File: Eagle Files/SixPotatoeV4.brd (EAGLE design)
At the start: 120 x 60 mm, 27 parts, among them J3 IMU, J4 ON/OFF, J5 GND, J6 3.3v

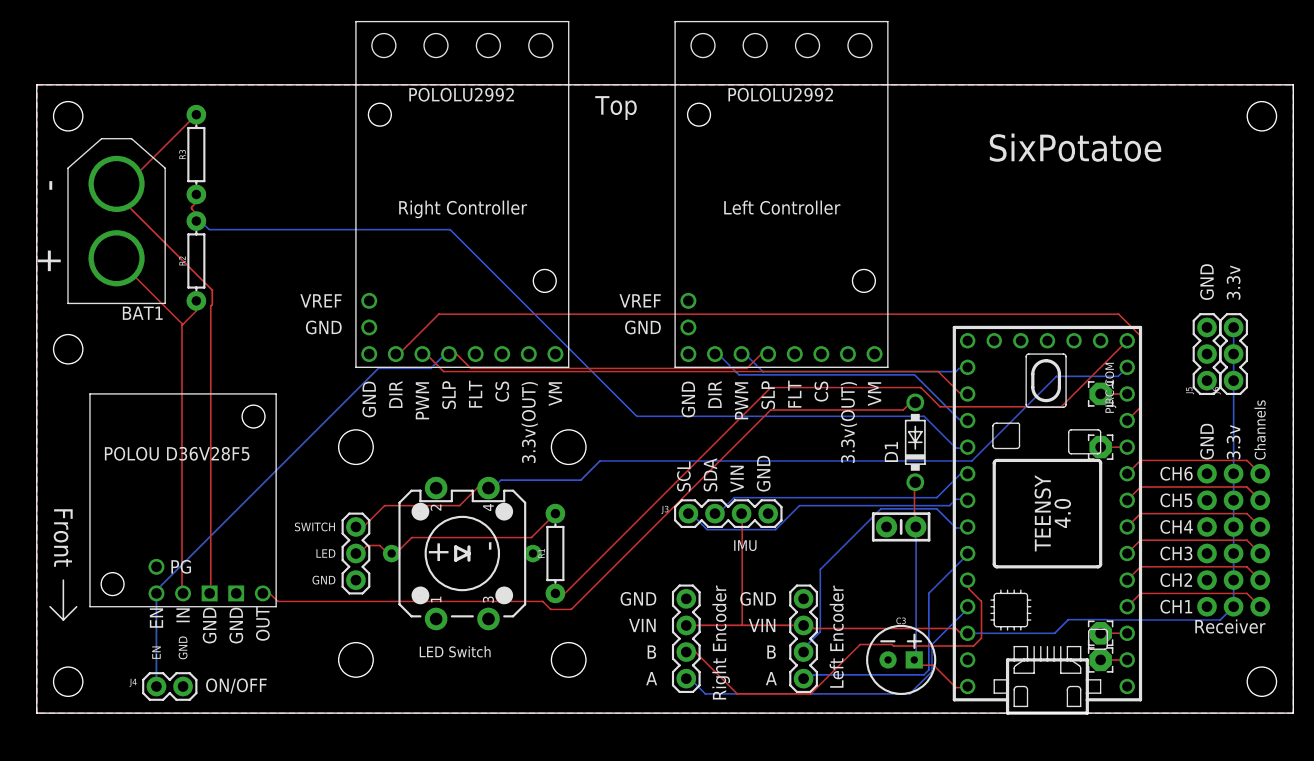
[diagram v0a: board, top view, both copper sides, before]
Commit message: Video completed
Also, excess code removed, first routes checked out.
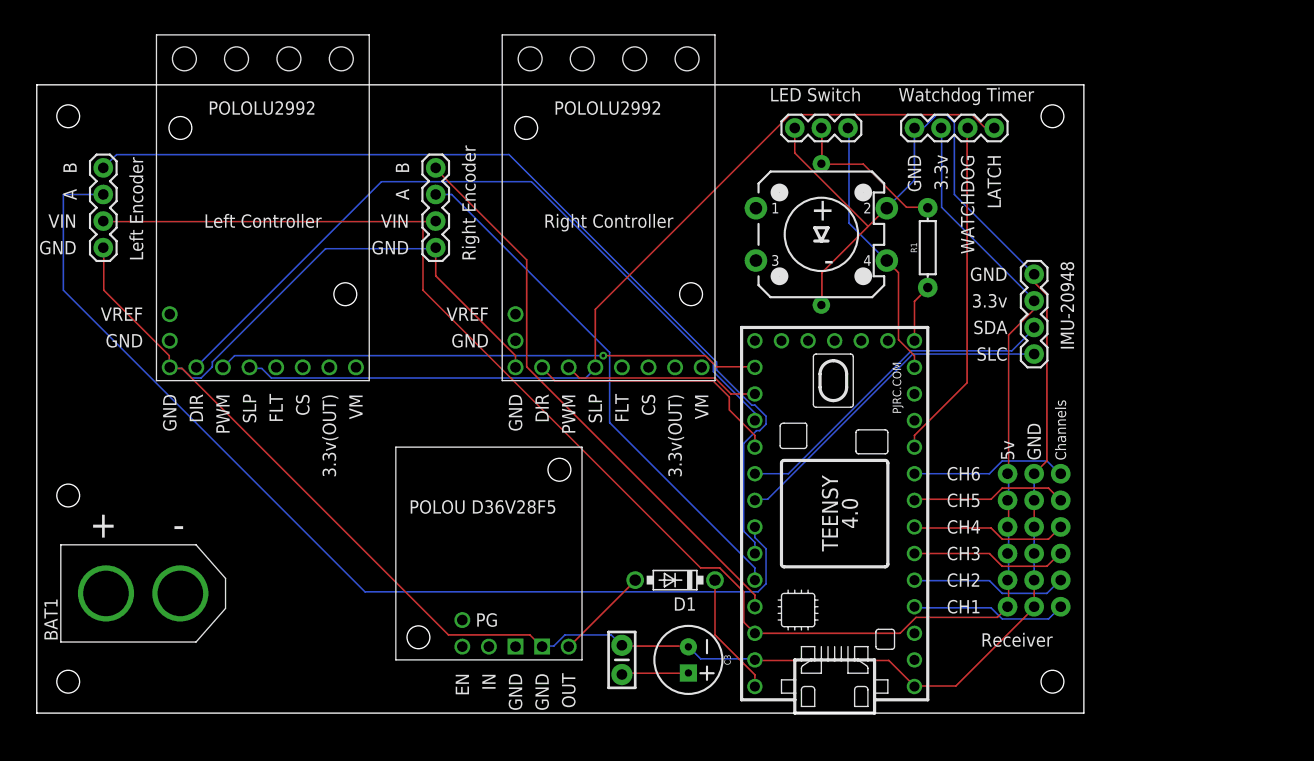
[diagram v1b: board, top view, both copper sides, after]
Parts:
- removed 0, 1, 10, 8: (no value), wirepad:2,15/1,0
- removed J4: ON/OFF, SparkFun-Connectors:1X02
- removed J5: GND, SparkFun-Connectors:1X03
- removed J6: 3.3v, SparkFun-Connectors:1X03
- removed R2, R3: 15k, SparkFun-Resistors:AXIAL-0.3
- removed U$5: SEN15335_NO_PTH, TimEagleLibrary:SEN15335_NO_PTH
- added J7: (no value), SparkFun-Connectors:1X04
- J3: value IMU -> (none)
- moved J2 74.8 mm to (6.35, 44.5), turned to 90 degrees
- moved J19 60.5 mm to (77.5, 55.9), turned to 180 degrees
- moved U$2 49.5 mm to (31.8, 64.8)
- moved R1 46.0 mm to (85.1, 44.5)
- moved S2 45.9 mm to (74.9, 45.7), turned to 0 degrees
- moved J1 41.2 mm to (38.1, 44.5), turned to 90 degrees
- moved J3 40.2 mm to (95.2, 41.9), turned to 270 degrees
- moved BAT1 35.7 mm to (10.2, 11.4), turned to 180 degrees
- moved U$4 29.6 mm to (43.2, 14.0)
- moved C2 29.5 mm to (55.9, 5.08), turned to 270 degrees
- moved D1 26.4 mm to (61.0, 12.7), turned to 180 degrees
- moved J9 21.6 mm to (92.7, 10.2)
- moved C3 20.3 mm to (62.2, 5.08), turned to 270 degrees
- moved U$1 20.3 mm to (76.2, 19.1)
- moved J8 19.0 mm to (97.8, 10.2)
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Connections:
- removed net ENABLE: J4.1, U$2.SLP, U$3.SLP, U$4.EN
- removed net GND2: BAT1.-, R3.P$2, U$4.GND2
- removed net N$5: 1.1, U$1.1/TX
- removed net N$6: 10.1, U$1.10/CS
- removed net N$7: 8.1, U$1.8
- removed net VMON: R2.P$2, R3.P$1, U$1.17/A3
- new net LATCH: J7.4, U$2.SLP, U$3.SLP
- new net V_BATT: BAT1.-
- new net V_GND: BAT1.+
- new net WATCHDOG: J7.3, U$1.8
- net 3.3V: now also J3.2, J7.2; no longer J3.3, J6.1, J6.2, J6.3
- net DIR_RIGHT: now also U$1.17/A3; no longer U$1.9/CS
- net GND: now also J3.1, J7.1; no longer J3.4, J4.2, J5.1, J5.2, J5.3
- net N$1: now also D1.C, U$1.VIN; no longer 0.1, U$1.0/RX
- net SCL: now also J3.4; no longer J3.1
- net SDA: now also J3.3; no longer J3.2
- net VBATT: no longer BAT1.+, R2.P$1
- net VIN: no longer D1.C, U$1.VIN
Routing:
- net GND: track 0.00 -> 247.3 mm
- net LATCH: track 0.00 -> 85.8 mm
- net VMON: track 85.7 -> 0.00 mm
- net ENABLE: track 78.1 -> 0.00 mm
- net B_LEFT: track 25.8 -> 98.2 mm
- net 3.3V: track 91.1 -> 161.6 mm
- net A_LEFT: track 25.0 -> 89.2 mm
- net 5V: track 71.1 -> 9.00 mm
- net N$3: track 66.1 -> 5.60 mm
- net DIR_RIGHT: track 82.2 -> 24.9 mm
- net N$4: track 80.0 -> 25.5 mm
- net GND2: track 53.5 -> 0.00 mm
- net DIR_LEFT: track 26.8 -> 71.0 mm
- net VBATT: track 37.6 -> 0.00 mm
- net PWM_RIGHT: track 53.6 -> 18.8 mm
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- removed copper zone on layer 1, net GND
- removed copper zone on layer 16, net GND
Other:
- board size 120 x 60 mm -> 100 x 60 mm
- board text added: "5v"
- board text added: "LATCH"
- board text added: "SLC"
- board text added: "WATCHDOG"
- board text added: "Watchdog Timer"
- board text removed: "0"
- board text removed: "1"
- board text removed: "10"
- board text removed: "3.3v(OUT)"
- board text removed: "8"
- board text removed: "Bottom"
- board text removed: "CS"
- board text removed: "DIR"
- board text removed: "FLT"
- board text removed: "Front"
- board text removed: "IMU"
- board text removed: "LED"
- board text removed: "ON/OFF"
- board text removed: "PWM"
- board text removed: "SCL"
- board text removed: "SLP"
- board text removed: "SWITCH"
- board text removed: "SixPotatoe"
- board text removed: "Top"
- board text removed: "VM"
